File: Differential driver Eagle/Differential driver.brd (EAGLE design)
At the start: 107.6 x 58.4 mm, 13 parts, among them IC1 7805TV, U1 SN75174N, U2 SN75174N

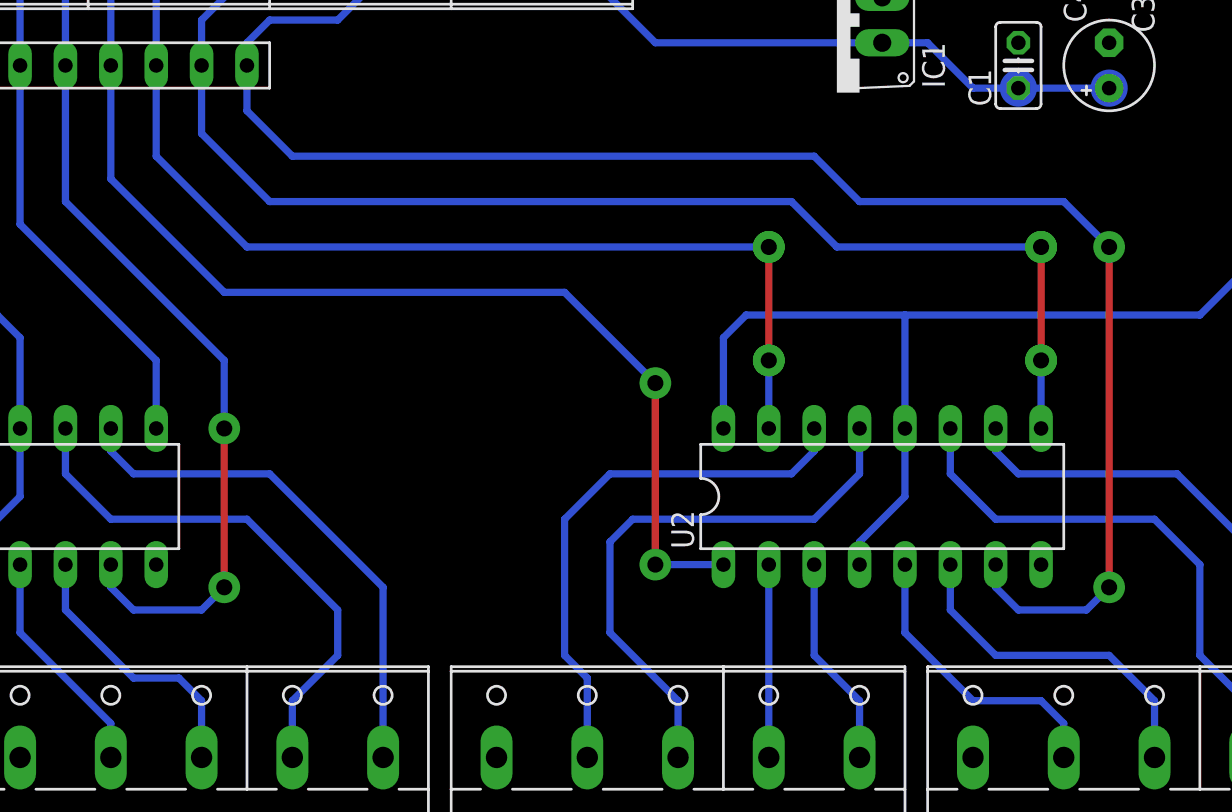
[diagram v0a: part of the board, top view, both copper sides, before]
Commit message: started electronics box
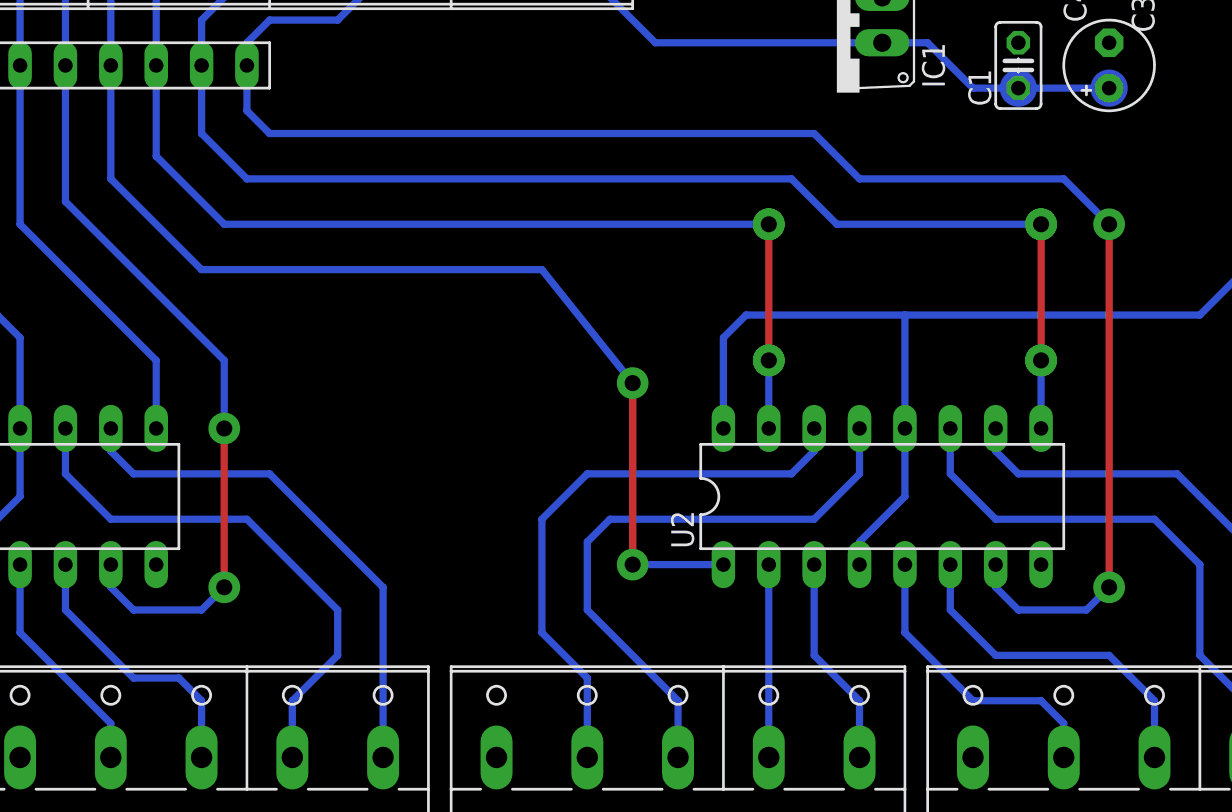
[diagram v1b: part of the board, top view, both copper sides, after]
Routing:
- net Z_DIR-: track 31.7 -> 33.5 mm
- net Z_DIR+: track 30.7 -> 32.5 mm
- net A_STEP: track 76.0 -> 76.7 mm
- net A_DIR: track 95.8 -> 96.6 mm
- net Z_DIR: track 61.5 -> 62.2 mm
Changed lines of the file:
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@@
 <param name="mtCopper" value="0.035mm 0.035mm 0.035mm 0.035mm 0.035mm 0.035mm 0.035mm 0.035mm 0.035mm 0.035mm 0.035mm 0.035mm 0.035mm 0.035mm 0.035mm 0.035mm"/>
 <param name="mtIsolate" value="1.5mm 0.15mm 0.2mm 0.15mm 0.2mm 0.15mm 0.2mm 0.15mm 0.2mm 0.15mm 0.2mm 0.15mm 0.2mm 0.15mm 0.2mm"/>
-<param name="mdWireWire" value="20mil"/>
-<param name="mdWirePad" value="20mil"/>
-<param name="mdWireVia" value="20mil"/>
+<param name="mdWireWire" value="16mil"/>
+<param name="mdWirePad" value="16mil"/>
+<param name="mdWireVia" value="16mil"/>
 <param name="mdPadPad" value="20mil"/>
 <param name="mdPadVia" value="20mil"/>
@@
 <param name="mdViaViaSameLayer" value="8mil"/>
 <param name="mnLayersViaInSmd" value="2"/>
-<param name="mdCopperDimension" value="20mil"/>
+<param name="mdCopperDimension" value="16mil"/>
 <param name="mdDrill" value="8mil"/>
 <param name="mdSmdStop" value="0mil"/>
@@
 <wire x1="31.75" y1="48.26" x2="31.75" y2="43.18" width="0.4064" layer="16"/>
 <contactref element="U2" pad="1"/>
-<wire x1="66.04" y1="15.24" x2="62.23" y2="15.24" width="0.4064" layer="16"/>
-<via x="62.23" y="15.24" extent="1-16" drill="0.9" diameter="1.6764"/>
-<wire x1="62.23" y1="15.24" x2="62.23" y2="25.4" width="0.4064" layer="1"/>
-<via x="62.23" y="25.4" extent="1-16" drill="0.9" diameter="1.6764"/>
-<wire x1="62.23" y1="25.4" x2="57.15" y2="30.48" width="0.4064" layer="16"/>
-<wire x1="57.15" y1="30.48" x2="38.1" y2="30.48" width="0.4064" layer="16"/>
-<wire x1="38.1" y1="30.48" x2="31.75" y2="36.83" width="0.4064" layer="16"/>
+<wire x1="66.04" y1="15.24" x2="60.96" y2="15.24" width="0.4064" layer="16"/>
+<via x="60.96" y="15.24" extent="1-16" drill="0.9" diameter="1.6764"/>
+<wire x1="60.96" y1="15.24" x2="60.96" y2="25.4" width="0.4064" layer="1"/>
+<via x="60.96" y="25.4" extent="1-16" drill="0.9" diameter="1.6764"/>
+<wire x1="60.96" y1="25.4" x2="55.88" y2="31.75" width="0.4064" layer="16"/>
+<wire x1="55.88" y1="31.75" x2="36.83" y2="31.75" width="0.4064" layer="16"/>
+<wire x1="36.83" y1="31.75" x2="31.75" y2="36.83" width="0.4064" layer="16"/>
 <wire x1="31.75" y1="36.83" x2="31.75" y2="43.18" width="0.4064" layer="16"/>
-<via x="62.23" y="25.4" extent="1-16" drill="0.8" diameter="1.778"/>
-<via x="62.23" y="15.24" extent="1-16" drill="0.8" diameter="1.778"/>
+<via x="60.96" y="25.4" extent="1-16" drill="0.8" diameter="1.778"/>
+<via x="60.96" y="15.24" extent="1-16" drill="0.8" diameter="1.778"/>
 </signal>
 <signal name="Z_DIR">
@@
 <wire x1="68.58" y1="22.86" x2="68.58" y2="26.67" width="0.4064" layer="16"/>
 <via x="68.58" y="26.67" extent="1-16" drill="0.9" diameter="1.778"/>
-<wire x1="68.58" y1="26.67" x2="68.58" y2="33.02" width="0.4064" layer="1"/>
-<via x="68.58" y="33.02" extent="1-16" drill="0.9" diameter="1.778"/>
-<wire x1="68.58" y1="33.02" x2="39.37" y2="33.02" width="0.4064" layer="16"/>
-<wire x1="39.37" y1="33.02" x2="34.29" y2="38.1" width="0.4064" layer="16"/>
+<wire x1="68.58" y1="26.67" x2="68.58" y2="34.29" width="0.4064" layer="1"/>
+<via x="68.58" y="34.29" extent="1-16" drill="0.9" diameter="1.778"/>
+<wire x1="68.58" y1="34.29" x2="38.1" y2="34.29" width="0.4064" layer="16"/>
+<wire x1="38.1" y1="34.29" x2="34.29" y2="38.1" width="0.4064" layer="16"/>
 <wire x1="34.29" y1="38.1" x2="34.29" y2="43.18" width="0.4064" layer="16"/>
 <via x="68.58" y="26.67" extent="1-16" drill="0.8" diameter="1.778"/>
-<via x="68.58" y="33.02" extent="1-16" drill="0.8" diameter="1.778"/>
+<via x="68.58" y="34.29" extent="1-16" drill="0.8" diameter="1.778"/>
 </signal>
 <signal name="A_STEP">
@@
 <contactref element="U2" pad="9"/>
 <contactref element="X5" pad="4"/>
-<wire x1="83.82" y1="33.02" x2="72.39" y2="33.02" width="0.4064" layer="16"/>
-<wire x1="72.39" y1="33.02" x2="69.85" y2="35.56" width="0.4064" layer="16"/>
-<wire x1="69.85" y1="35.56" x2="40.64" y2="35.56" width="0.4064" layer="16"/>
-<wire x1="40.64" y1="35.56" x2="36.83" y2="39.37" width="0.4064" layer="16"/>
+<wire x1="83.82" y1="34.29" x2="72.39" y2="34.29" width="0.4064" layer="16"/>
+<wire x1="72.39" y1="34.29" x2="69.85" y2="36.83" width="0.4064" layer="16"/>
+<wire x1="69.85" y1="36.83" x2="39.37" y2="36.83" width="0.4064" layer="16"/>
+<wire x1="39.37" y1="36.83" x2="36.83" y2="39.37" width="0.4064" layer="16"/>
 <wire x1="36.83" y1="39.37" x2="36.83" y2="43.18" width="0.4064" layer="16"/>
 <wire x1="43.18" y1="51.435" x2="43.18" y2="49.53" width="0.4064" layer="16"/>
@@
 <wire x1="83.82" y1="22.86" x2="83.82" y2="26.67" width="0.4064" layer="16"/>
 <via x="83.82" y="26.67" extent="1-16" drill="0.9" diameter="1.778"/>
-<wire x1="83.82" y1="26.67" x2="83.82" y2="33.02" width="0.4064" layer="1"/>
-<via x="83.82" y="33.02" extent="1-16" drill="0.9" diameter="1.778"/>
-<via x="83.82" y="33.02" extent="1-16" drill="0.8" diameter="1.778"/>
+<wire x1="83.82" y1="26.67" x2="83.82" y2="34.29" width="0.4064" layer="1"/>
+<via x="83.82" y="34.29" extent="1-16" drill="0.9" diameter="1.778"/>
+<via x="83.82" y="34.29" extent="1-16" drill="0.8" diameter="1.778"/>
 <via x="83.82" y="26.67" extent="1-16" drill="0.8" diameter="1.778"/>
 </signal>
@@
 <wire x1="86.36" y1="12.7" x2="87.63" y2="13.97" width="0.4064" layer="16"/>
 <via x="87.63" y="13.97" extent="1-16" drill="0.9" diameter="1.6764"/>
-<wire x1="87.63" y1="13.97" x2="87.63" y2="33.02" width="0.4064" layer="1"/>
-<via x="87.63" y="33.02" extent="1-16" drill="0.9" diameter="1.6764"/>
-<wire x1="87.63" y1="33.02" x2="85.09" y2="35.56" width="0.4064" layer="16"/>
-<wire x1="85.09" y1="35.56" x2="73.66" y2="35.56" width="0.4064" layer="16"/>
-<wire x1="73.66" y1="35.56" x2="71.12" y2="38.1" width="0.4064" layer="16"/>
-<wire x1="71.12" y1="38.1" x2="41.91" y2="38.1" width="0.4064" layer="16"/>
-<wire x1="41.91" y1="38.1" x2="39.37" y2="40.64" width="0.4064" layer="16"/>
+<wire x1="87.63" y1="13.97" x2="87.63" y2="34.29" width="0.4064" layer="1"/>
+<via x="87.63" y="34.29" extent="1-16" drill="0.9" diameter="1.6764"/>
+<wire x1="87.63" y1="34.29" x2="85.09" y2="36.83" width="0.4064" layer="16"/>
+<wire x1="85.09" y1="36.83" x2="73.66" y2="36.83" width="0.4064" layer="16"/>
+<wire x1="73.66" y1="36.83" x2="71.12" y2="39.37" width="0.4064" layer="16"/>
+<wire x1="71.12" y1="39.37" x2="40.64" y2="39.37" width="0.4064" layer="16"/>
+<wire x1="40.64" y1="39.37" x2="39.37" y2="40.64" width="0.4064" layer="16"/>
 <wire x1="39.37" y1="40.64" x2="39.37" y2="43.18" width="0.4064" layer="16"/>
 <wire x1="48.26" y1="51.435" x2="48.26" y2="49.53" width="0.4064" layer="16"/>
@@
 <wire x1="40.64" y1="45.72" x2="39.37" y2="44.45" width="0.4064" layer="16"/>
 <wire x1="39.37" y1="44.45" x2="39.37" y2="43.18" width="0.4064" layer="16"/>
-<via x="87.63" y="33.02" extent="1-16" drill="0.8" diameter="1.778"/>
+<via x="87.63" y="34.29" extent="1-16" drill="0.8" diameter="1.778"/>
 <via x="87.63" y="13.97" extent="1-16" drill="0.8" diameter="1.778"/>
 </signal>
@@
 <contactref element="X3" pad="2"/>
 <wire x1="58.42" y1="4.445" x2="58.42" y2="8.89" width="0.4064" layer="16"/>
-<wire x1="58.42" y1="8.89" x2="57.15" y2="10.16" width="0.4064" layer="16"/>
-<wire x1="57.15" y1="10.16" x2="57.15" y2="17.78" width="0.4064" layer="16"/>
-<wire x1="57.15" y1="17.78" x2="59.69" y2="20.32" width="0.4064" layer="16"/>
-<wire x1="59.69" y1="20.32" x2="69.85" y2="20.32" width="0.4064" layer="16"/>
+<wire x1="58.42" y1="8.89" x2="55.88" y2="11.43" width="0.4064" layer="16"/>
+<wire x1="55.88" y1="11.43" x2="55.88" y2="17.78" width="0.4064" layer="16"/>
+<wire x1="55.88" y1="17.78" x2="58.42" y2="20.32" width="0.4064" layer="16"/>
+<wire x1="58.42" y1="20.32" x2="69.85" y2="20.32" width="0.4064" layer="16"/>
 <wire x1="69.85" y1="20.32" x2="71.12" y2="21.59" width="0.4064" layer="16"/>
 <wire x1="71.12" y1="21.59" x2="71.12" y2="22.86" width="0.4064" layer="16"/>
@@
 <contactref element="X3" pad="3"/>
 <wire x1="63.5" y1="4.445" x2="63.5" y2="7.62" width="0.4064" layer="16"/>
-<wire x1="63.5" y1="7.62" x2="59.69" y2="11.43" width="0.4064" layer="16"/>
-<wire x1="59.69" y1="11.43" x2="59.69" y2="16.51" width="0.4064" layer="16"/>
-<wire x1="59.69" y1="16.51" x2="60.96" y2="17.78" width="0.4064" layer="16"/>
-<wire x1="60.96" y1="17.78" x2="71.12" y2="17.78" width="0.4064" layer="16"/>
+<wire x1="63.5" y1="7.62" x2="58.42" y2="12.7" width="0.4064" layer="16"/>
+<wire x1="58.42" y1="12.7" x2="58.42" y2="16.51" width="0.4064" layer="16"/>
+<wire x1="58.42" y1="16.51" x2="59.69" y2="17.78" width="0.4064" layer="16"/>
+<wire x1="59.69" y1="17.78" x2="71.12" y2="17.78" width="0.4064" layer="16"/>
 <wire x1="71.12" y1="17.78" x2="73.66" y2="20.32" width="0.4064" layer="16"/>
 <wire x1="73.66" y1="20.32" x2="73.66" y2="22.86" width="0.4064" layer="16"/>

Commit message: driver update
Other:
- board size 107.6 x 58.4 mm -> 110.2 x 58.4 mm
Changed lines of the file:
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@@
 <layer number="17" name="Pads" color="2" fill="1" visible="yes" active="yes"/>
 <layer number="18" name="Vias" color="2" fill="1" visible="yes" active="yes"/>
-<layer number="19" name="Unrouted" color="6" fill="1" visible="yes" active="yes"/>
-<layer number="20" name="Dimension" color="15" fill="1" visible="yes" active="yes"/>
+<layer number="19" name="Unrouted" color="6" fill="1" visible="no" active="yes"/>
+<layer number="20" name="Dimension" color="15" fill="1" visible="no" active="yes"/>
 <layer number="21" name="tPlace" color="7" fill="1" visible="no" active="yes"/>
 <layer number="22" name="bPlace" color="7" fill="1" visible="no" active="yes"/>
@@
 <layer number="43" name="vRestrict" color="2" fill="10" visible="no" active="yes"/>
 <layer number="44" name="Drills" color="7" fill="1" visible="no" active="yes"/>
-<layer number="45" name="Holes" color="7" fill="1" visible="yes" active="yes"/>
+<layer number="45" name="Holes" color="7" fill="1" visible="no" active="yes"/>
 <layer number="46" name="Milling" color="3" fill="1" visible="no" active="yes"/>
 <layer number="47" name="Measures" color="7" fill="1" visible="no" active="yes"/>
-<layer number="48" name="Document" color="7" fill="1" visible="yes" active="yes"/>
+<layer number="48" name="Document" color="7" fill="1" visible="no" active="yes"/>
 <layer number="49" name="Reference" color="7" fill="1" visible="no" active="yes"/>
 <layer number="51" name="tDocu" color="7" fill="1" visible="no" active="yes"/>
@@
 <board>
 <plain>
-<wire x1="-3.81" y1="-1.27" x2="103.81" y2="-1.27" width="0" layer="20"/>
-<wire x1="103.81" y1="-1.27" x2="103.81" y2="57.14" width="0" layer="20"/>
-<wire x1="103.81" y1="57.14" x2="-3.81" y2="57.14" width="0" layer="20"/>
-<wire x1="-3.81" y1="57.14" x2="-3.81" y2="-1.27" width="0" layer="20"/>
+<wire x1="-5.08" y1="-1.27" x2="105.08" y2="-1.27" width="0" layer="20"/>
+<wire x1="105.08" y1="-1.27" x2="105.08" y2="57.14" width="0" layer="20"/>
+<wire x1="105.08" y1="57.14" x2="-5.08" y2="57.14" width="0" layer="20"/>
+<wire x1="-5.08" y1="57.14" x2="-5.08" y2="-1.27" width="0" layer="20"/>
 <hole x="0" y="13.97" drill="3.2"/>
 <hole x="100.33" y="13.97" drill="3.2"/>
-<hole x="100.33" y="53.34" drill="3.2"/>
-<hole x="0" y="53.34" drill="3.2"/>
-<dimension x1="-3.81" y1="57.14" x2="103.81" y2="57.14" x3="50" y3="60.96" textsize="1.778" layer="47"/>
-<dimension x1="-3.81" y1="57.14" x2="-3.81" y2="-1.27" x3="-7.62" y3="27.935" textsize="1.778" layer="47"/>
+<hole x="100.33" y="52.07" drill="3.2"/>
+<hole x="0" y="52.07" drill="3.2"/>
+<dimension x1="-3.81" y1="57.14" x2="-3.81" y2="-1.27" x3="-13.97" y3="27.935" textsize="1.778" layer="47"/>
 <circle x="82.55" y="50.8" radius="0.635" width="0.8128" layer="16"/>
 <circle x="87.63" y="50.8" radius="0.635" width="0.8128" layer="16"/>
 <circle x="87.63" y="41.91" radius="0.635" width="0.8128" layer="16"/>
 <circle x="82.55" y="41.91" radius="0.635" width="0.8128" layer="16"/>
+<dimension x1="-5.08" y1="57.15" x2="105.41" y2="57.15" x3="50.165" y3="66.04" textsize="1.778" layer="47"/>
+<dimension x1="0" y1="49.53" x2="100.33" y2="49.53" x3="50.165" y3="60.96" textsize="1.778" layer="47" dtype="diameter"/>
+<dimension x1="3.81" y1="13.97" x2="3.81" y2="52.07" x3="-8.89" y3="33.02" textsize="1.778" layer="47" dtype="diameter"/>
+<dimension x1="0" y1="48.26" x2="-5.08" y2="48.26" x3="-2.54" y3="62.23" textsize="1.778" layer="47" dtype="diameter"/>
+<dimension x1="3.81" y1="52.07" x2="3.81" y2="57.15" x3="-10.16" y3="54.61" textsize="1.778" layer="47" dtype="diameter"/>
 </plain>
 <attributes>
@@
 <contactref element="X5" pad="2"/>
 <polygon width="0.4064" layer="16" orphans="yes">
-<vertex x="-3.81" y="57.15"/>
-<vertex x="104.14" y="57.15"/>
-<vertex x="104.14" y="-1.27"/>
-<vertex x="-3.81" y="-1.27"/>
+<vertex x="-5.08" y="57.15"/>
+<vertex x="105.41" y="57.15"/>
+<vertex x="105.41" y="-1.27"/>
+<vertex x="-5.08" y="-1.27"/>
 </polygon>
 </signal>
